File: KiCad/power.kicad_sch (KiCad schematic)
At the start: 13 parts, among them J4 10-pin power header, U1 TL074

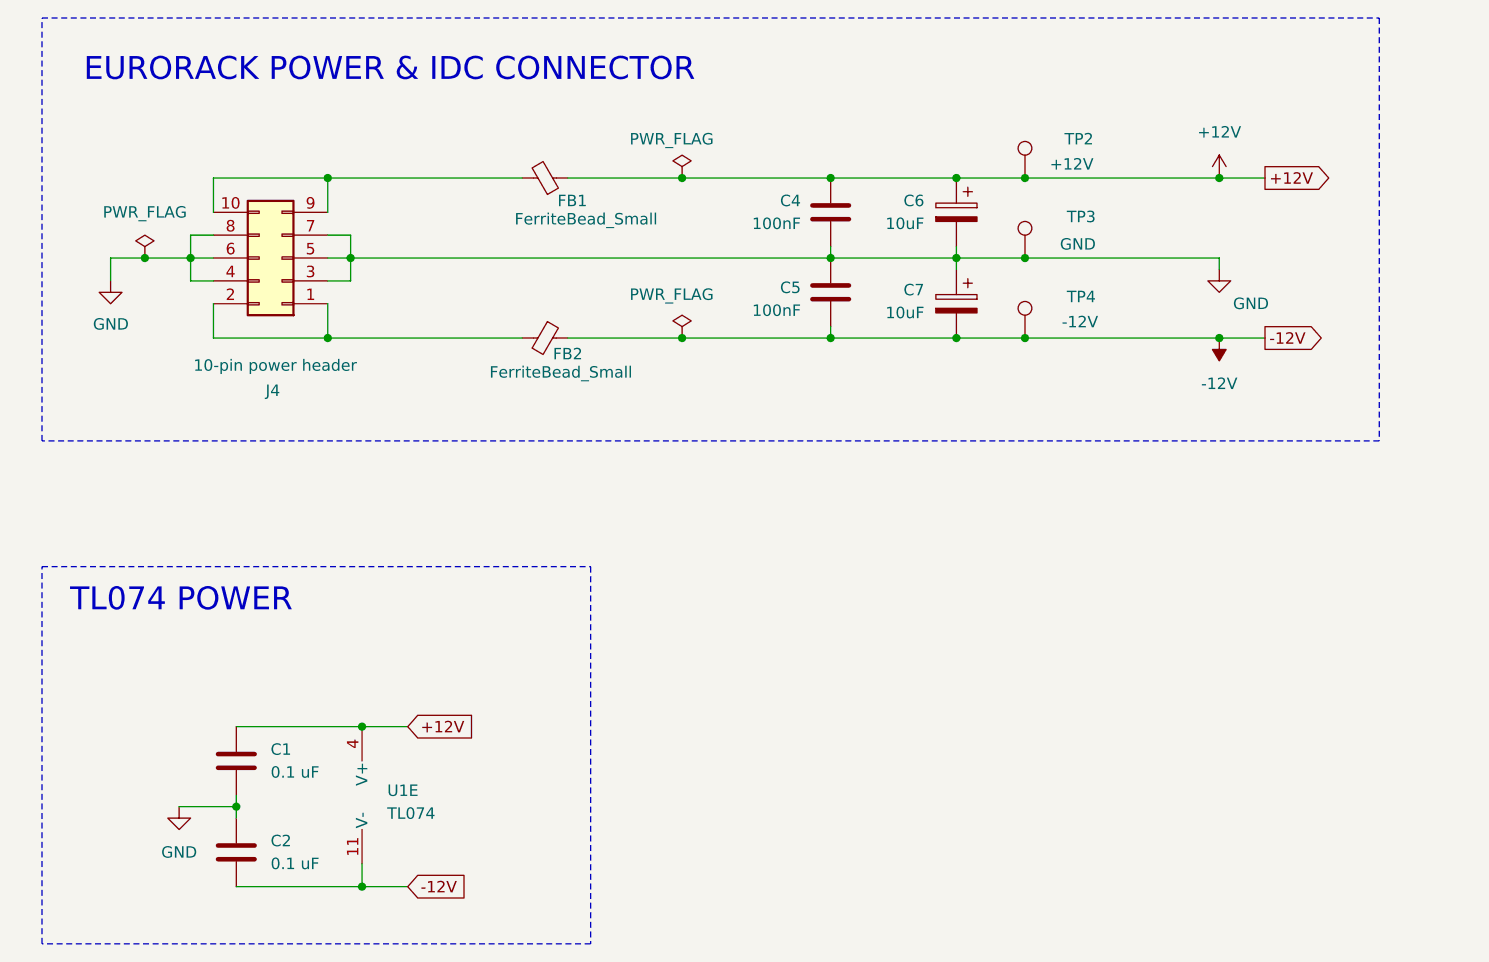
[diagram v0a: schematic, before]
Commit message: refactor(kicad): move switch/LED driver logic into switches_led sheet
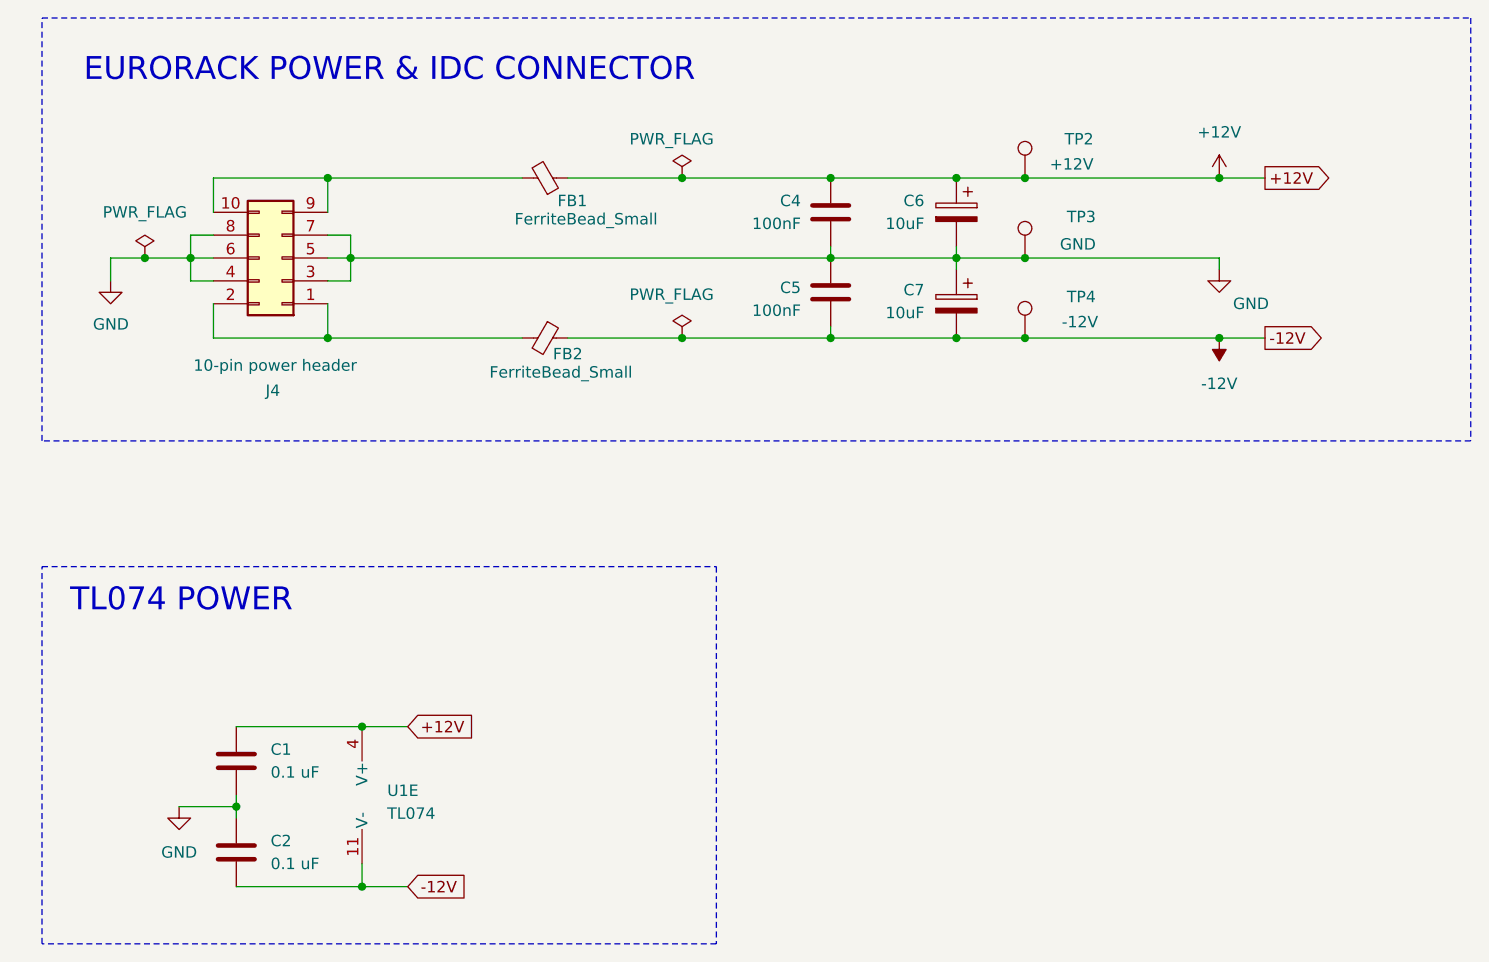
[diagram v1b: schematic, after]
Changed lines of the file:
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@@
 	(rectangle
 		(start 16.51 21.59)
-		(end 165.1 68.58)
+		(end 175.26 68.58)
 		(stroke
 			(width 0)
@@
 	(rectangle
 		(start 16.51 82.55)
-		(end 77.47 124.46)
+		(end 91.44 124.46)
 		(stroke
 			(width 0)

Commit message: Refine KiCad schematics for power, test points, and control values
  - replace schematic +12V/-12V global labels with proper power symbols
  - add GND test points and reorganize the power/IDC and main sequencer
  sheets
  - retune sequencer values including R33/R34 to 51k, R35 to 68k, C8 to
  1nF, and trim pots to 2k/5k
  - update switch/LED sheet labels and pot values, renaming LEDs by step
  and changing B250k controls to B100k
  - relax the KiCad four-way junction ERC setting in the project file
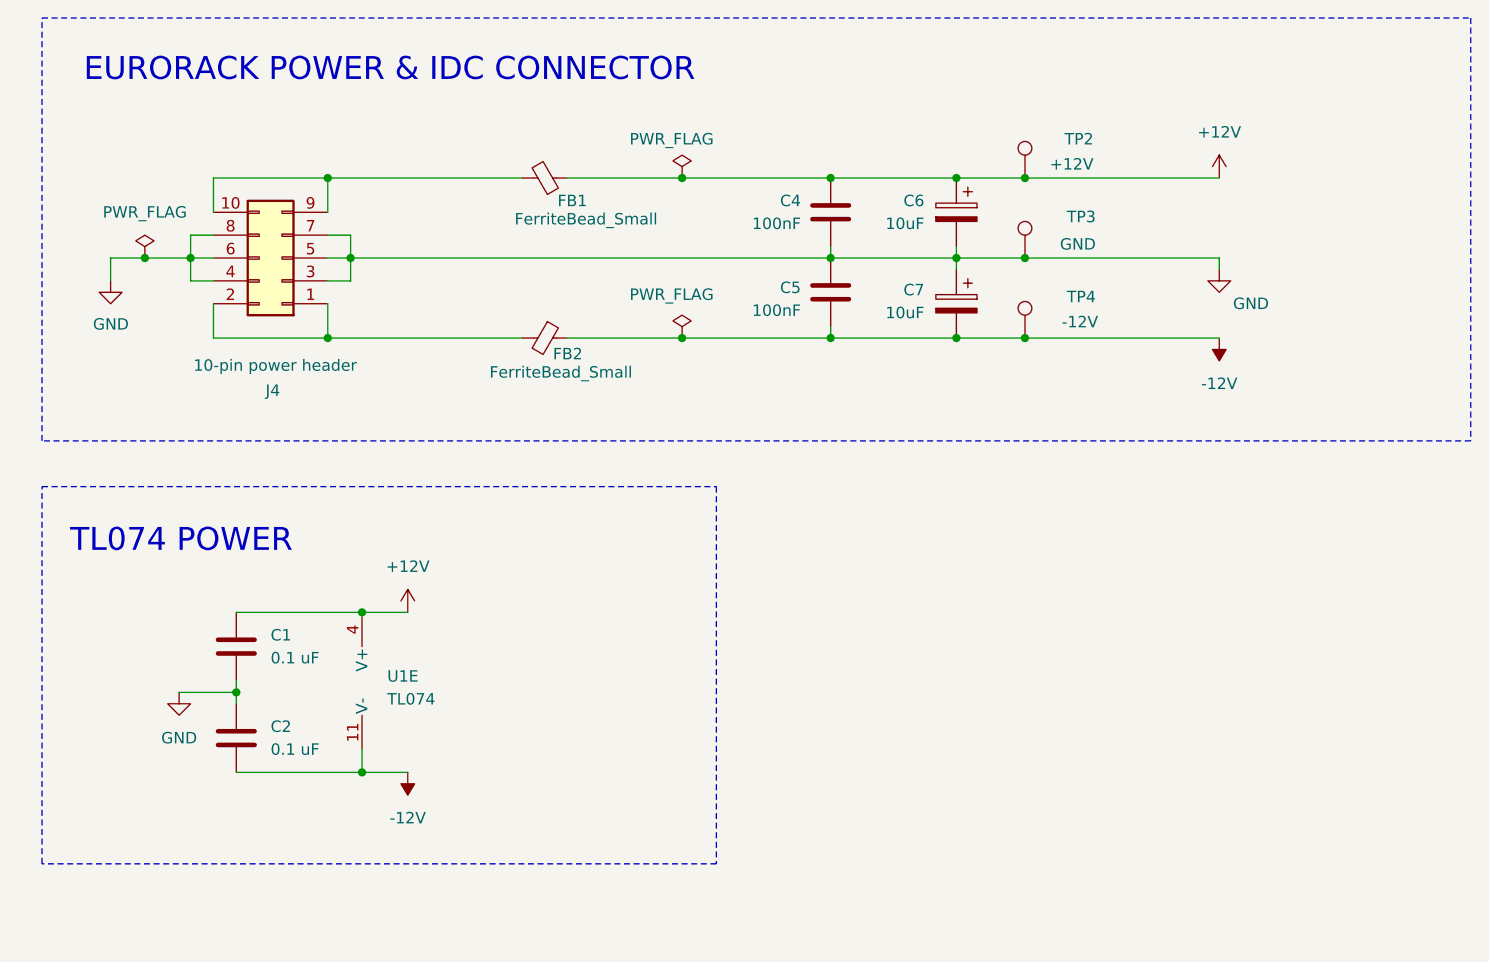
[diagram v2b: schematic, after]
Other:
- moved on the sheet: C1, C2, U1E

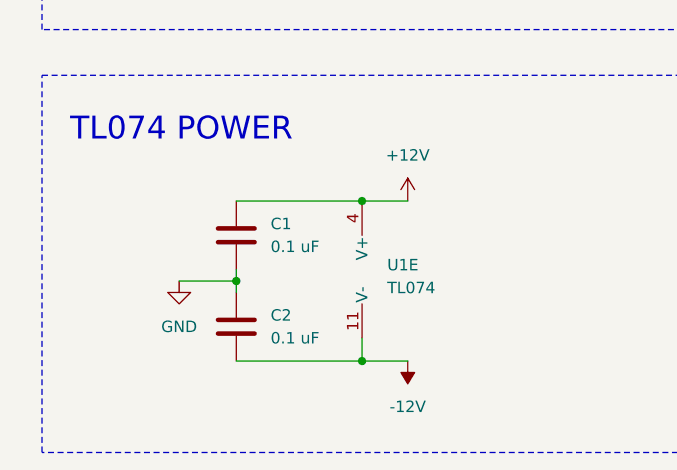
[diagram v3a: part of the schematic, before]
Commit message: adding missing footprints to the power supply
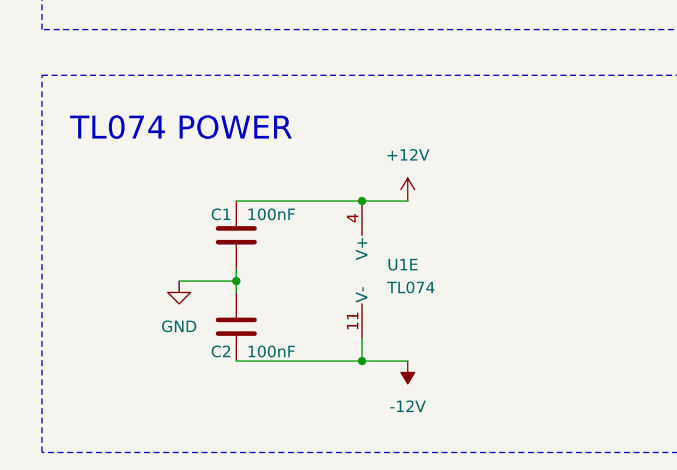
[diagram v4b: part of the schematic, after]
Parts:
- C1, C2: value 0.1 uF -> 100nF; footprint (none) -> Capacitor_SMD:C_0805_2012Metric_Pad1.18x1.45mm_HandSolder
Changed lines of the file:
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@@
-	)
-	(symbol
-		(lib_id "Device:C")
-		(at 38.1 101.6 0)
-		(unit 1)
-		(exclude_from_sim no)
-		(in_bom yes)
-		(on_board yes)
-		(dnp no)
-		(fields_autoplaced yes)
-		(property "Reference" "C2"
-			(at 41.91 100.3299 0)
-			(effects
-				(font
-					(size 1.27 1.27)
-				)
-				(justify left)
-			)
-		)
-		(property "Value" "0.1 uF"
-			(at 41.91 102.8699 0)
-			(effects
-				(font
-					(size 1.27 1.27)
-				)
-				(justify left)
-			)
-		)
-		(property "Footprint" ""
-			(at 39.0652 105.41 0)
-			(effects
-				(font
-					(size 1.27 1.27)
-				)
-				(hide yes)
-			)
-		)
-		(property "Datasheet" "~"
-			(at 38.1 101.6 0)
-			(effects
-				(font
-					(size 1.27 1.27)
-				)
-				(hide yes)
-			)
-		)
-		(property "Description" "Unpolarized capacitor"
-			(at 38.1 101.6 0)
-			(effects
-				(font
-					(size 1.27 1.27)
-				)
-				(hide yes)
-			)
-		)
-		(pin "1"
-		)
-		(pin "2"
-		)
-		(instances
-			(project "sequencer"
-				(path "/c997e785-a132-463f-bd08-a5a67a697207/6da73ad2-1669-4740-9ebd-dad26a4437f2"
-					(reference "C2")
-					(unit 1)
-				)
-			)
-		)
 	)
 	(symbol
@@
 	)
 	(symbol
+		(lib_id "Device:C")
+		(at 38.1 101.6 0)
+		(mirror y)
+		(unit 1)
+		(exclude_from_sim no)
+		(in_bom yes)
+		(on_board yes)
+		(dnp no)
+		(property "Reference" "C2"
+			(at 37.592 104.394 0)
+			(effects
+				(font
+					(size 1.27 1.27)
+				)
+				(justify left)
+			)
+		)
+		(property "Value" "100nF"
+			(at 44.704 104.394 0)
+			(effects
+				(font
+					(size 1.27 1.27)
+				)
+				(justify left)
+			)
+		)
+		(property "Footprint" "Capacitor_SMD:C_0805_2012Metric_Pad1.18x1.45mm_HandSolder"
+			(at 37.1348 105.41 0)
+			(effects
+				(font
+					(size 1.27 1.27)
+				)
+				(hide yes)
+			)
+		)
+		(property "Datasheet" "https://www.taydaelectronics.com/100nf-50v-smd-ceramic-chip-capacitor.html"
+			(at 38.1 101.6 0)
+			(effects
+				(font
+					(size 1.27 1.27)
+				)
+				(hide yes)
+			)
+		)
+		(property "Description" "Unpolarized capacitor"
+			(at 38.1 101.6 0)
+			(effects
+				(font
+					(size 1.27 1.27)
+				)
+				(hide yes)
+			)
+		)
+		(pin "2"
+		)
+		(pin "1"
+		)
+		(instances
+			(project "sequencer"
+				(path "/c997e785-a132-463f-bd08-a5a67a697207/6da73ad2-1669-4740-9ebd-dad26a4437f2"
+					(reference "C2")
+					(unit 1)
+				)
+			)
+		)
+	)
+	(symbol
 		(lib_id "Device:C_Polarized")
 		(at 118.11 53.34 0)
@@
 	)
 	(symbol
+		(lib_id "Device:C")
+		(at 38.1 91.44 0)
+		(mirror y)
+		(unit 1)
+		(exclude_from_sim no)
+		(in_bom yes)
+		(on_board yes)
+		(dnp no)
+		(property "Reference" "C1"
+			(at 37.592 89.154 0)
+			(effects
+				(font
+					(size 1.27 1.27)
+				)
+				(justify left)
+			)
+		)
+		(property "Value" "100nF"
+			(at 44.704 89.154 0)
+			(effects
+				(font
+					(size 1.27 1.27)
+				)
+				(justify left)
+			)
+		)
+		(property "Footprint" "Capacitor_SMD:C_0805_2012Metric_Pad1.18x1.45mm_HandSolder"
+			(at 37.1348 95.25 0)
+			(effects
+				(font
+					(size 1.27 1.27)
+				)
+				(hide yes)
+			)
+		)
+		(property "Datasheet" "https://www.taydaelectronics.com/100nf-50v-smd-ceramic-chip-capacitor.html"
+			(at 38.1 91.44 0)
+			(effects
+				(font
+					(size 1.27 1.27)
+				)
+				(hide yes)
+			)
+		)
+		(property "Description" "Unpolarized capacitor"
+			(at 38.1 91.44 0)
+			(effects
+				(font
+					(size 1.27 1.27)
+				)
+				(hide yes)
+			)
+		)
+		(pin "2"
+		)
+		(pin "1"
+		)
+		(instances
+			(project "sequencer"
+				(path "/c997e785-a132-463f-bd08-a5a67a697207/6da73ad2-1669-4740-9ebd-dad26a4437f2"
+					(reference "C1")
+					(unit 1)
+				)
+			)
+		)
+	)
+	(symbol
 		(lib_id "power:+12V")
 		(at 57.15 87.63 0)
@@
 					(unit 1)
 				)
-			)
-		)
-	)
-	(symbol
-		(lib_id "Device:C")
-		(at 38.1 91.44 0)
-		(unit 1)
-		(exclude_from_sim no)
-		(in_bom yes)
-		(on_board yes)
-		(dnp no)
-		(fields_autoplaced yes)
-		(property "Reference" "C1"
-			(at 41.91 90.1699 0)
-			(effects
-				(font
-					(size 1.27 1.27)
-				)
-				(justify left)
-			)
-		)
-		(property "Value" "0.1 uF"
-			(at 41.91 92.7099 0)
-			(effects
-				(font
-					(size 1.27 1.27)
-				)
-				(justify left)
-			)
-		)
-		(property "Footprint" ""
-			(at 39.0652 95.25 0)
-			(effects
-				(font
-					(size 1.27 1.27)
-				)
-				(hide yes)
-			)
-		)
-		(property "Datasheet" "~"
-			(at 38.1 91.44 0)
-			(effects
-				(font
-					(size 1.27 1.27)
-				)
-				(hide yes)
-			)
-		)
-		(property "Description" "Unpolarized capacitor"
-			(at 38.1 91.44 0)
-			(effects
-				(font
-					(size 1.27 1.27)
-				)
-				(hide yes)
-			)
-		)
-		(pin "1"
-		)
-		(pin "2"
-		)
-		(instances
-			(project "sequencer"
-				(path "/c997e785-a132-463f-bd08-a5a67a697207/6da73ad2-1669-4740-9ebd-dad26a4437f2"
-					(reference "C1")
-					(unit 1)
-				)

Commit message: adding missing SMD footprints
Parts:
- U1: footprint (none) -> Package_SO:SOIC-14_3.9x8.7mm_P1.27mm
